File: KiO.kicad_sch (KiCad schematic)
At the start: 9 parts, among them J2 Conn_01x04_Socket_LED, J3 Conn_01x02_Socket_Motor, U1 XIAO-ESP32-S3-DIP, U2 L293D, U3 HC-SR04, U4 DM-OLED096-636

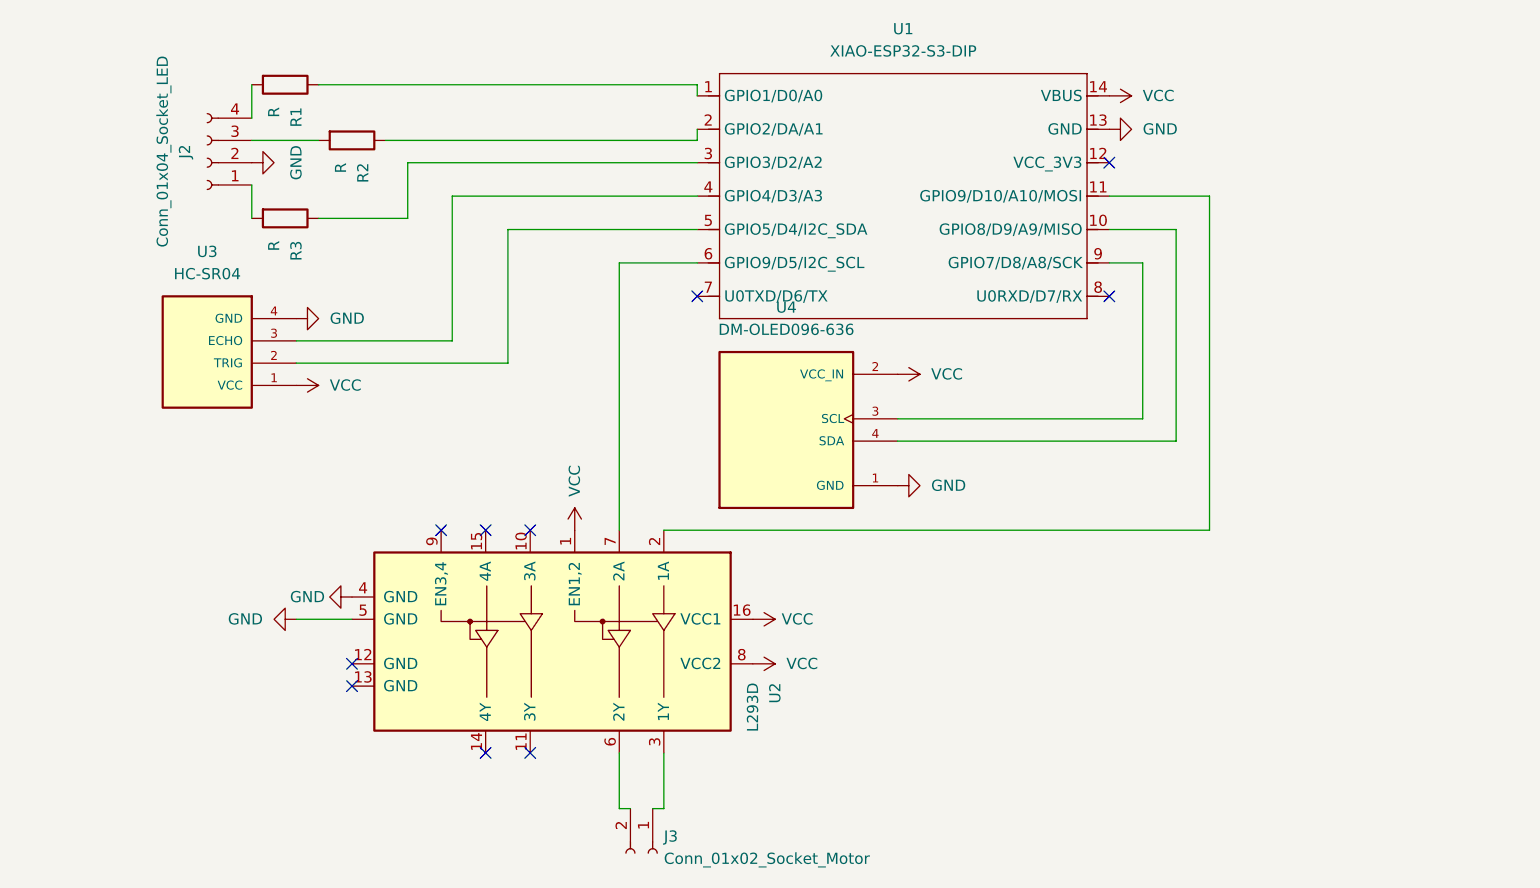
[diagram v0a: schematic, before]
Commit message: fix screen display and connection
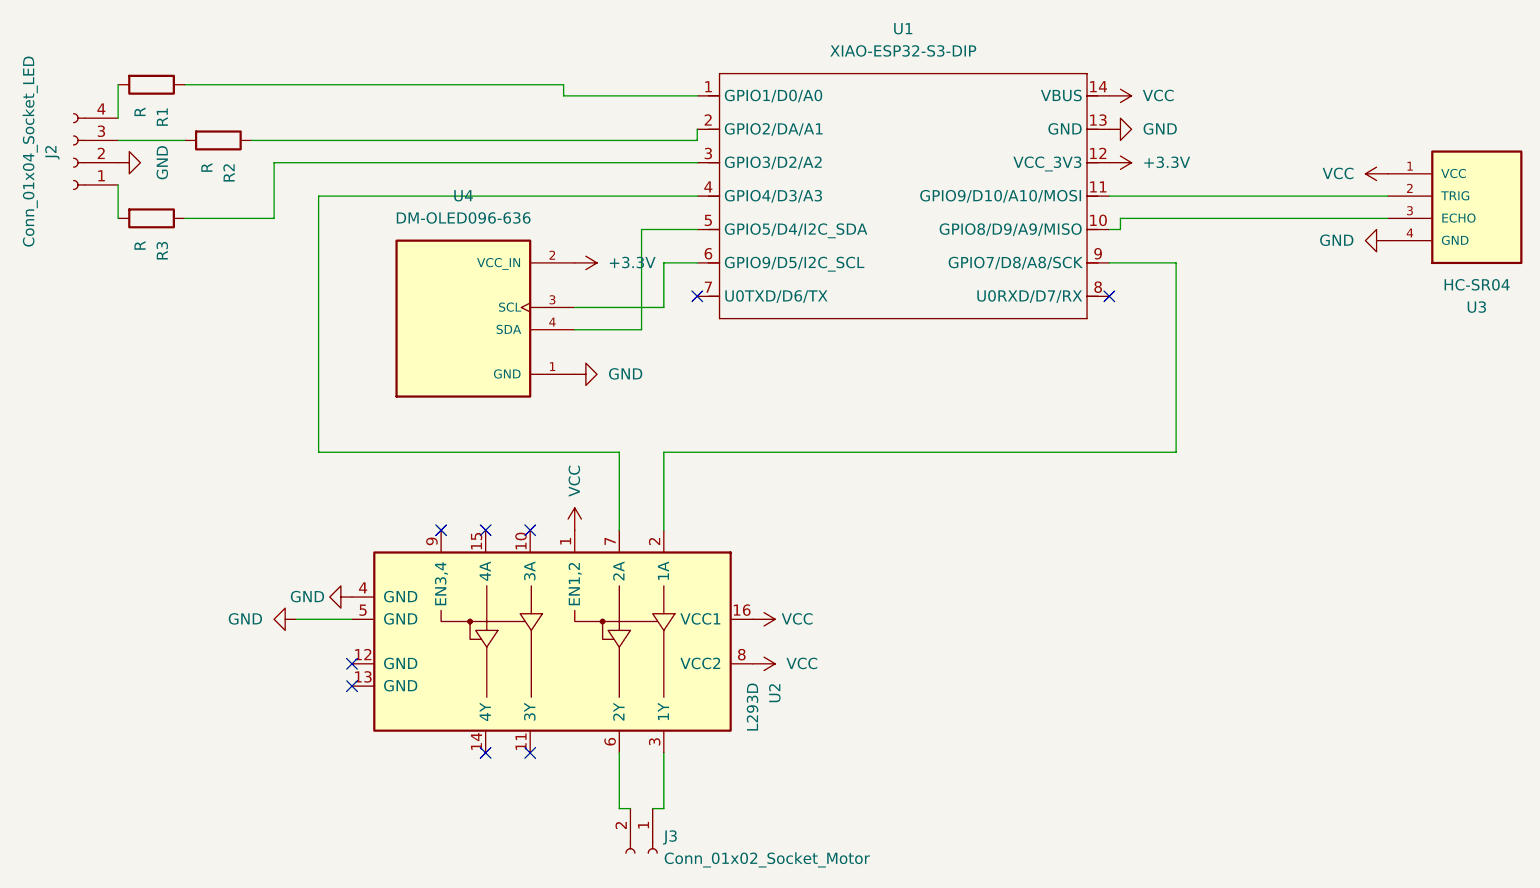
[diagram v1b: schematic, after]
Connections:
- net VCC: no longer U4.2 (VCC_IN)
- net at U2.2 (1A): now also U1.9 (GPIO7/D8/A8/SCK); no longer U1.11 (GPIO9/D10/A10/MOSI)
- net at U2.7 (2A): now also U1.4 (GPIO4/D3/A3); no longer U1.6 (GPIO9/D5/I2C_SCL)
- net at U1.10 (GPIO8/D9/A9/MISO): now also U3.3 (ECHO); no longer U4.4 (SDA)
- net +3.3V: now reaches U1.12 (VCC_3V3)
- net +3.3V: now also U4.2 (VCC_IN)
- net at U3.2 (TRIG): now also U1.11 (GPIO9/D10/A10/MOSI); no longer U1.5 (GPIO5/D4/I2C_SDA)
- net at U4.3 (SCL): now also U1.6 (GPIO9/D5/I2C_SCL); no longer U1.9 (GPIO7/D8/A8/SCK)
- new net: U1.5 (GPIO5/D4/I2C_SDA), U4.4 (SDA)
- no-connect marks 10 -> 9
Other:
- moved on the sheet: J2, R1, R2, R3, U3, U4
